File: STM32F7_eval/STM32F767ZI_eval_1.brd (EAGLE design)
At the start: 76.2 x 53.3 mm, 102 parts, among them CN1 STLINKV2_SWD_IF_, CN2 GROVE-4P-CONN-I2C-90D, CN3 GROVE-4P-CONN-I2C-90D, CN5 ARDUINO_COMPAT_IF, CN7 WFT0750CZ09-SMD_, CN9 UART_IF, Q1 PMF370XN_, SW1 SKRPACE010_, SW2 SKRPACE010_, U1 STM32F767ZI_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

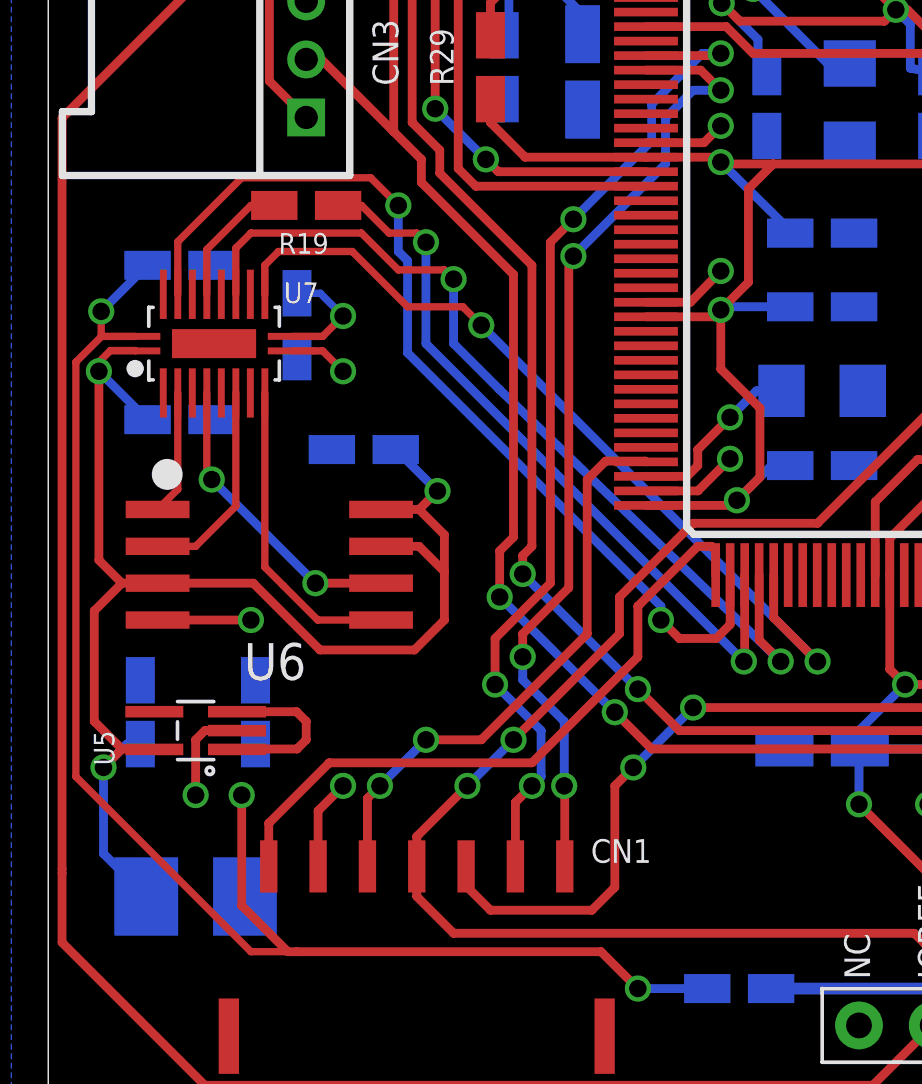
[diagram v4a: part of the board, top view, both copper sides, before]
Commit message: レイアウトを修正
・デザインルールチェック済み第１版
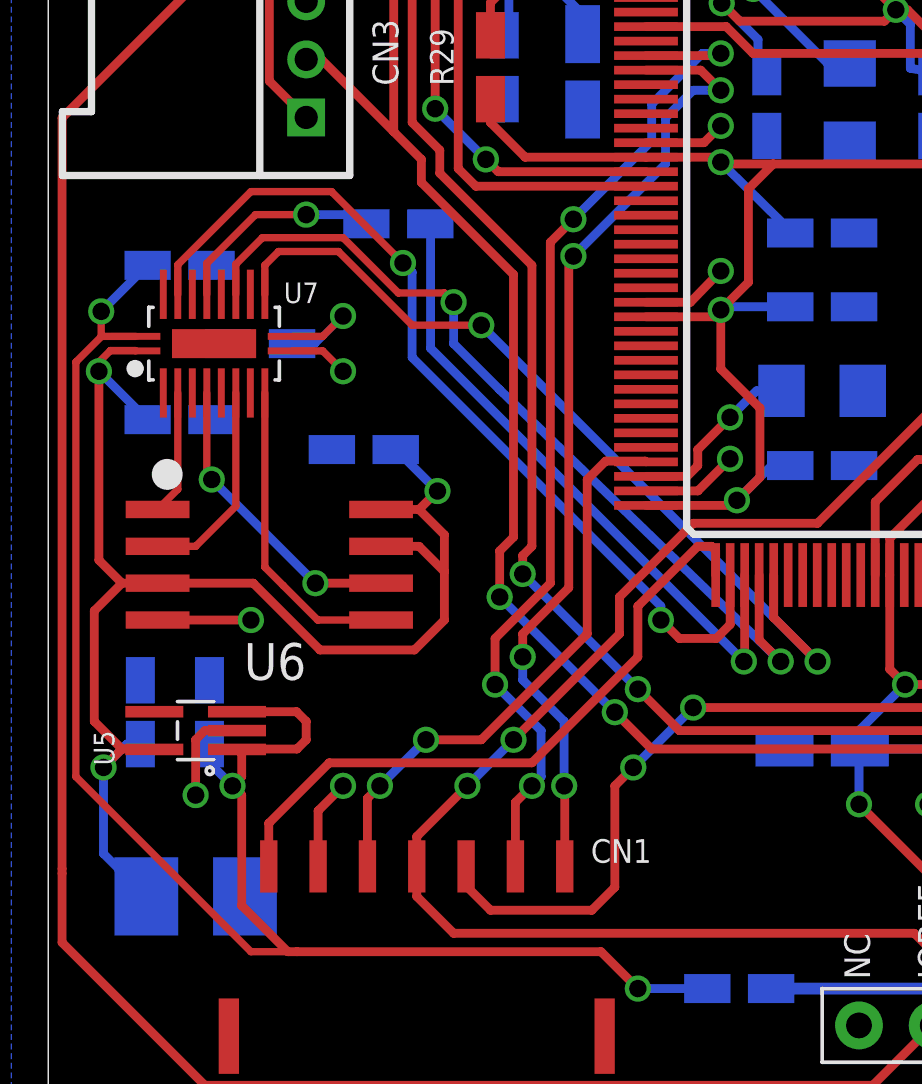
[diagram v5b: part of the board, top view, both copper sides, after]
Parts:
- moved R19 3.24 mm to (12.1, 30.2), flipped to the bottom, turned to 180 degrees
- moved C49 1.59 mm to (5.56, 13.3)
- moved R5 1.42 mm to (7.30, 26.0), turned to 180 degrees
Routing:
- net VCC_MEM: track 56.7 -> 60.4 mm
- net PC10: track 25.5 -> 22.5 mm, vias 2 -> 1
- net PC10_D: track 4.50 -> 7.39 mm, vias 0 -> 1
- net PA15: track 33.3 -> 31.4 mm
- net PC11: track 31.2 -> 30.3 mm

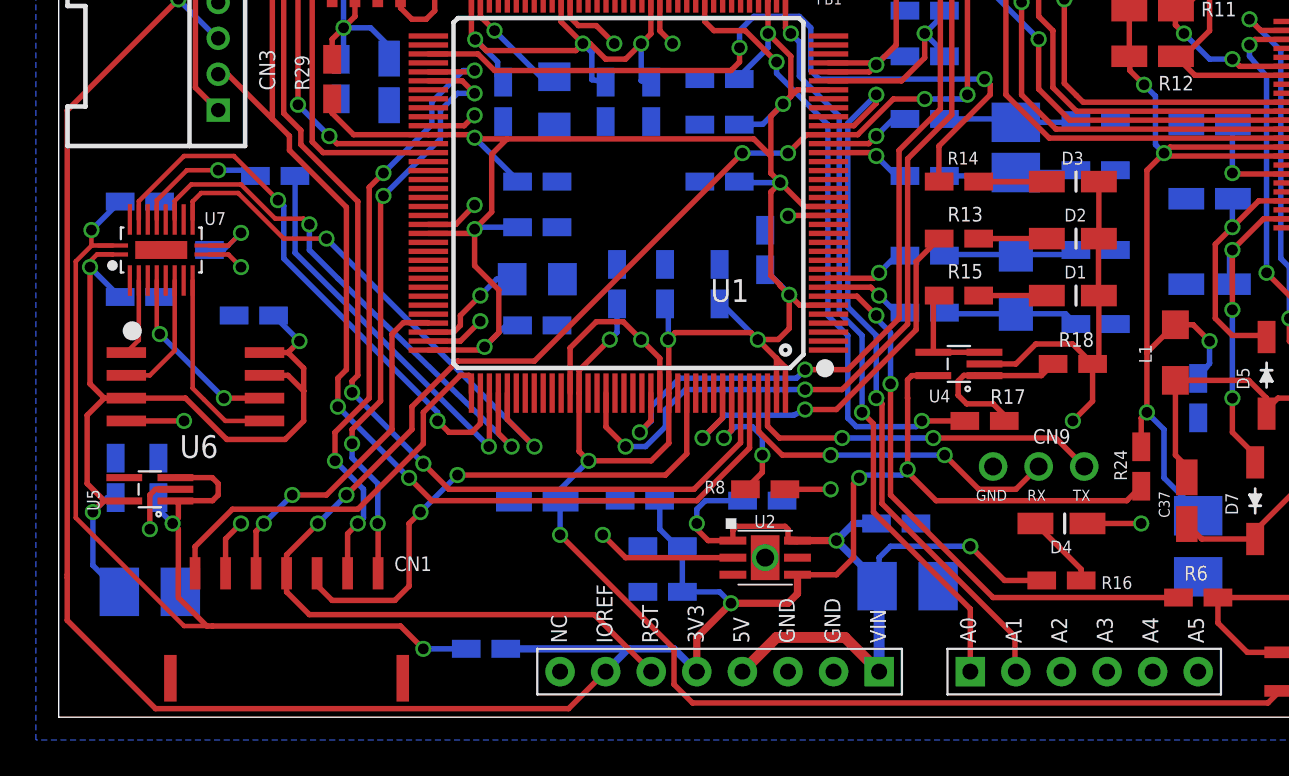
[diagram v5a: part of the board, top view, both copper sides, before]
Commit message: レイアウトを修正
・通信モジュール用のUARTピンの位置を変更
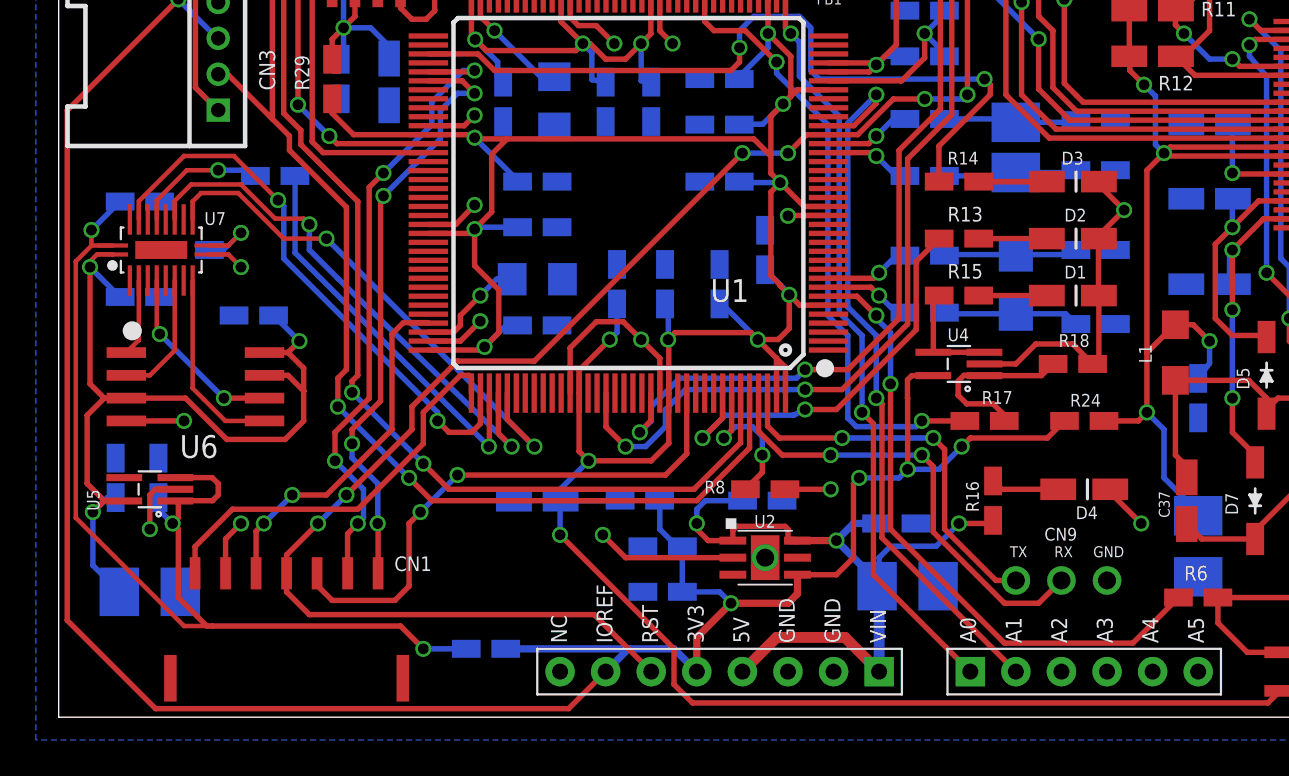
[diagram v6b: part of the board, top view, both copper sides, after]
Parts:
- moved CN9 8.98 mm to (58.4, 7.62), turned to 180 degrees
- moved R16 5.85 mm to (52.1, 12.1), turned to 270 degrees
- moved R24 4.07 mm to (57.1, 16.5), turned to 0 degrees
- moved D4 2.29 mm to (57.1, 12.7)
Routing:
- net PE0: track 19.6 -> 25.6 mm
- net +3V3: track 147.0 -> 143.2 mm, vias 4 -> 5
- net PC13: track 31.8 -> 35.1 mm
- net VIN: track 47.1 -> 44.2 mm
- net 0V: track 175.5 -> 172.6 mm
- net PE1: track 20.4 -> 21.8 mm
- net VCC_EPD: track 60.1 -> 60.6 mm

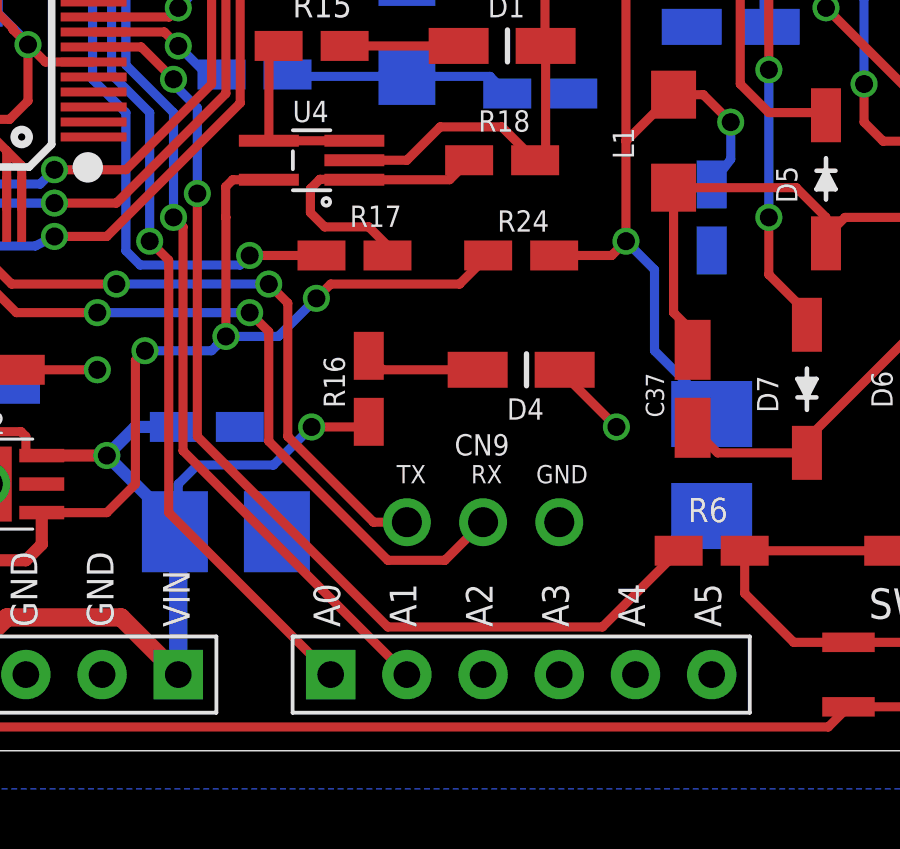
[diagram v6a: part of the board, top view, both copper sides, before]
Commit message: レイアウトを修正
・外部RX、TXはArduinoアナログピンを流用させるよう実装変更
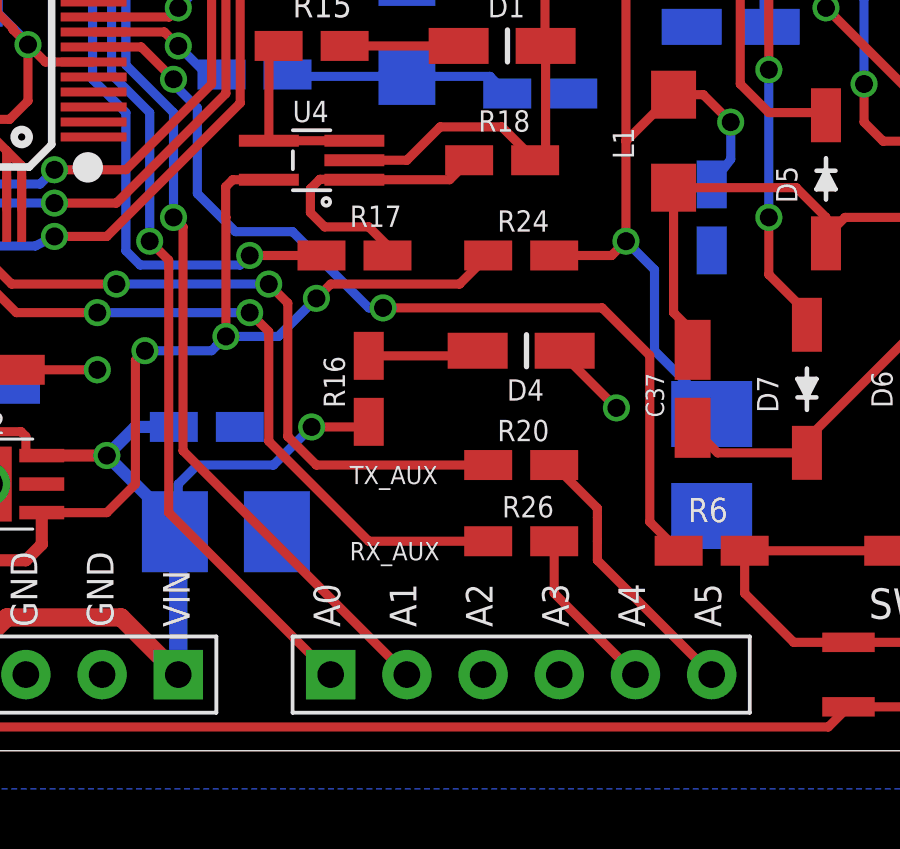
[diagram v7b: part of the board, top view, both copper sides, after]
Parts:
- removed CN9: UART_IF, PartsForProto:UART_IF_3PIN
- added R20, R26: 0, Parts:SMD_1608_DEV
- moved D4 0.64 mm to (57.1, 13.3)
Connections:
- new net RX_AUX: CN5.31, R26.1
- new net TX_AUX: CN5.32, R20.1
- net 0V: no longer CN9.1
- net PE0: now also R26.2; no longer CN9.2
- net PE1: now also R20.2; no longer CN9.3
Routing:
- net TX_AUX: track 0.00 -> 9.16 mm
- net RX_AUX: track 0.00 -> 5.57 mm
- net PC13: track 35.1 -> 31.5 mm
- net PE1: track 21.8 -> 23.8 mm
- net 0V: track 172.6 -> 171.5 mm
- net PE0: track 25.6 -> 25.0 mm
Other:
- board text added: "RX_AUX"
- board text added: "TX_AUX"
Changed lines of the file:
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@@
 <setting verticaltext="up"/>
 </settings>
-<grid distance="0.05" unitdist="inch" unit="inch" style="lines" multiple="1" display="yes" altdistance="0.025" altunitdist="inch" altunit="inch"/>
+<grid distance="0.05" unitdist="inch" unit="mil" style="lines" multiple="1" display="yes" altdistance="0.025" altunitdist="inch" altunit="inch"/>
 <layers>
 <layer number="1" name="Top" color="4" fill="1" visible="yes" active="yes"/>
@@
 <circle x="42.70375" y="19.446875" radius="0.508" width="0" layer="21"/>
 <circle x="63.02375" y="43.259375" radius="0.4064" width="0" layer="21"/>
+<text x="51.435" y="8.89" size="0.6096" layer="25">TX_AUX</text>
+<text x="51.435" y="6.35" size="0.6096" layer="25">RX_AUX</text>
 </plain>
 <attributes>
@@
 <attribute name="VALUE" x="50.8" y="25.4" size="0.8128" layer="27" rot="R180"/>
 </element>
-<element name="D4" library="Parts" package="CHIPLED_0805" value="LED_0805" x="57.15" y="12.7" smashed="yes">
-<attribute name="NAME" x="56.67375" y="11.7475" size="0.7112" layer="25" align="top-left"/>
-<attribute name="VALUE" x="54.61" y="11.1125" size="0.7112" layer="27"/>
+<element name="D4" library="Parts" package="CHIPLED_0805" value="LED_0805" x="57.15" y="13.335" smashed="yes">
+<attribute name="NAME" x="56.67375" y="12.3825" size="0.7112" layer="25" align="top-left"/>
+<attribute name="VALUE" x="54.61" y="11.7475" size="0.7112" layer="27"/>
 </element>
 <element name="R16" library="Parts" package="SMD_1608_DEV" value="1k" x="52.07" y="12.065" smashed="yes" rot="R270">
@@
 <attribute name="NAME" x="56.35625" y="17.30375" size="0.7112" layer="25"/>
 <attribute name="VALUE" x="56.515" y="14.605" size="0.8128" layer="27"/>
-</element>
-<element name="CN9" library="PartsForProto" package="UART_IF_3PIN" value="UART_IF" x="58.42" y="7.62" smashed="yes" rot="R180">
-<attribute name="NAME" x="54.9275" y="9.8425" size="0.7112" layer="25" ratio="10"/>
-<attribute name="VALUE" x="59.3725" y="10.795" size="0.8128" layer="27" rot="R180"/>
 </element>
 <element name="C39" library="Parts" package="C1210_TPST_DEV" value="10uF" x="63.5" y="9.525" smashed="yes" rot="MR270">
@@
 <element name="CN2" library="PartsForProto" package="GROVE-4P-90D" value="GROVE-4P-CONN-I2C-90D" x="8.89" y="47.9425" rot="R90"/>
 <element name="CN3" library="PartsForProto" package="GROVE-4P-90D" value="GROVE-4P-CONN-I2C-90D" x="8.89" y="36.83" rot="R90"/>
+<element name="R20" library="Parts" package="SMD_1608_DEV" value="0" x="57.15" y="9.525" smashed="yes" rot="R180">
+<attribute name="NAME" x="56.35625" y="10.31875" size="0.7112" layer="25"/>
+<attribute name="VALUE" x="57.785" y="11.43" size="0.8128" layer="27" rot="R180"/>
+</element>
+<element name="R26" library="Parts" package="SMD_1608_DEV" value="0" x="57.15" y="6.985" smashed="yes" rot="R180">
+<attribute name="NAME" x="56.515" y="7.77875" size="0.7112" layer="25"/>
+<attribute name="VALUE" x="57.785" y="8.89" size="0.8128" layer="27" rot="R180"/>
+</element>
 </elements>
 <signals>
@@
 <wire x1="29.96" y1="38.54" x2="30.96" y2="37.54" width="0.3048" layer="1"/>
 <via x="40.64" y="27.94" extent="1-16" drill="0.6"/>
-<wire x1="49.0075" y1="7.3025" x2="49.53" y2="8.255" width="0.6096" layer="16"/>
 <wire x1="72.91" y1="51.875" x2="68.06" y2="51.875" width="0.3048" layer="1"/>
 <via x="74.295" y="5.3975" extent="1-16" drill="0.6"/>
@@
 <contactref element="C38" pad="2"/>
 <contactref element="D6" pad="1"/>
-<contactref element="CN9" pad="1"/>
 <wire x1="74.295" y1="36.195" x2="74.295" y2="37.465" width="0.3048" layer="1"/>
 <wire x1="70.485" y1="9.93" x2="73.46" y2="9.93" width="0.3048" layer="1"/>
@@
 <contactref element="CN2" pad="4"/>
 <contactref element="CN3" pad="4"/>
-<via x="60.325" y="10.795" extent="1-16" drill="0.6"/>
+<via x="60.325" y="11.43" extent="1-16" drill="0.6"/>
 <via x="43.02125" y="12.7" extent="1-16" drill="0.6"/>
 <wire x1="40.47" y1="12.7" x2="43.02125" y2="12.7" width="0.3048" layer="1"/>
@@
 <wire x1="57.965" y1="26.67" x2="57.965" y2="26.85" width="0.3048" layer="1"/>
 <wire x1="57.965" y1="26.85" x2="59.3725" y2="28.2575" width="0.3048" layer="1"/>
-<wire x1="60.325" y1="10.795" x2="58.6" y2="12.52" width="0.3048" layer="1"/>
-<wire x1="58.6" y1="12.52" x2="58.6" y2="12.7" width="0.3048" layer="1"/>
+<wire x1="58.6" y1="13.335" x2="58.6" y2="13.155" width="0.3048" layer="1"/>
+<wire x1="58.6" y1="13.155" x2="60.325" y2="11.43" width="0.3048" layer="1"/>
 </signal>
 <signal name="N$2">
@@
 <contactref element="R6" pad="1"/>
 <via x="45.56125" y="22.38375" extent="1-16" drill="0.6"/>
-<via x="46.355" y="18.57375" extent="1-16" drill="0.6"/>
 <wire x1="46.355" y1="21.43125" x2="46.355" y2="18.57375" width="0.3048" layer="16"/>
 <wire x1="45.56125" y1="22.38375" x2="45.56125" y2="22.225" width="0.3048" layer="16"/>
@@
 <wire x1="42.9" y1="23.46" x2="44.485" y2="23.46" width="0.3048" layer="1"/>
 <wire x1="44.485" y1="23.46" x2="45.56125" y2="22.38375" width="0.3048" layer="1"/>
-<wire x1="46.355" y1="18.57375" x2="46.355" y2="10.4775" width="0.3048" layer="1"/>
-<wire x1="46.355" y1="10.4775" x2="52.705" y2="4.1275" width="0.3048" layer="1"/>
-<wire x1="52.705" y1="4.1275" x2="59.86" y2="4.1275" width="0.3048" layer="1"/>
-<wire x1="59.86" y1="4.1275" x2="62.4" y2="6.6675" width="0.3048" layer="1"/>
+<wire x1="62.4" y1="6.6675" x2="61.43625" y2="7.63125" width="0.3048" layer="1"/>
+<wire x1="61.43625" y1="7.63125" x2="61.43625" y2="13.17625" width="0.3048" layer="1"/>
+<wire x1="61.43625" y1="13.17625" x2="59.84875" y2="14.76375" width="0.3048" layer="1"/>
+<wire x1="59.84875" y1="14.76375" x2="52.54625" y2="14.76375" width="0.3048" layer="1"/>
+<via x="52.54625" y="14.76375" extent="1-16" drill="0.6"/>
+<wire x1="52.54625" y1="14.76375" x2="52.07" y2="14.76375" width="0.3048" layer="16"/>
+<wire x1="52.07" y1="14.76375" x2="49.53" y2="17.30375" width="0.3048" layer="16"/>
+<wire x1="49.53" y1="17.30375" x2="47.625" y2="17.30375" width="0.3048" layer="16"/>
+<wire x1="47.625" y1="17.30375" x2="46.355" y2="18.57375" width="0.3048" layer="16"/>
 </signal>
 <signal name="AGND">
@@
 <contactref element="R16" pad="1"/>
 <contactref element="D4" pad="A"/>
-<wire x1="52.07" y1="13.165" x2="52.535" y2="12.7" width="0.3048" layer="1"/>
-<wire x1="52.535" y1="12.7" x2="55.7" y2="12.7" width="0.3048" layer="1"/>
+<wire x1="52.07" y1="13.165" x2="55.53" y2="13.165" width="0.3048" layer="1"/>
+<wire x1="55.53" y1="13.165" x2="55.7" y2="13.335" width="0.3048" layer="1"/>
 </signal>
 <signal name="LED1">
@@
 <wire x1="43.65625" y1="15.5575" x2="40.16375" y2="15.5575" width="0.3048" layer="1"/>
 <wire x1="40.16375" y1="15.5575" x2="39.5" y2="16.22125" width="0.3048" layer="1"/>
-<contactref element="CN9" pad="3"/>
 <wire x1="48.73625" y1="15.5575" x2="49.37125" y2="14.9225" width="0.3048" layer="1"/>
 <wire x1="49.37125" y1="14.9225" x2="49.37125" y2="10.4775" width="0.3048" layer="1"/>
-<wire x1="49.37125" y1="10.4775" x2="52.22875" y2="7.62" width="0.3048" layer="1"/>
-<wire x1="52.22875" y1="7.62" x2="53.34" y2="7.62" width="0.3048" layer="1"/>
+<contactref element="R20" pad="2"/>
+<wire x1="56.05" y1="9.525" x2="50.32375" y2="9.525" width="0.3048" layer="1"/>
+<wire x1="50.32375" y1="9.525" x2="49.37125" y2="10.4775" width="0.3048" layer="1"/>
 </signal>
 <signal name="PE0">
@@
 <wire x1="43.02125" y1="14.605" x2="40.3225" y2="14.605" width="0.3048" layer="1"/>
 <wire x1="40.3225" y1="14.605" x2="39" y2="15.9275" width="0.3048" layer="1"/>
-<contactref element="CN9" pad="2"/>
 <wire x1="48.10125" y1="14.605" x2="48.73625" y2="13.97" width="0.3048" layer="1"/>
 <wire x1="48.73625" y1="13.97" x2="48.73625" y2="10.31875" width="0.3048" layer="1"/>
-<wire x1="48.73625" y1="10.31875" x2="52.705" y2="6.35" width="0.3048" layer="1"/>
-<wire x1="52.705" y1="6.35" x2="54.61" y2="6.35" width="0.3048" layer="1"/>
-<wire x1="54.61" y1="6.35" x2="55.88" y2="7.62" width="0.3048" layer="1"/>
+<contactref element="R26" pad="2"/>
+<wire x1="56.05" y1="6.985" x2="52.07" y2="6.985" width="0.3048" layer="1"/>
+<wire x1="52.07" y1="6.985" x2="48.73625" y2="10.31875" width="0.3048" layer="1"/>
 </signal>
 <signal name="VCC_EPD">
@@
 <wire x1="7.14375" y1="30.48" x2="8.89" y2="30.48" width="0.254" layer="1"/>
 </signal>
+<signal name="TX_AUX">
+<contactref element="CN5" pad="32"/>
+<contactref element="R20" pad="1"/>
+<wire x1="63.5" y1="2.54" x2="59.69" y2="6.35" width="0.3048" layer="1"/>
+<wire x1="59.69" y1="6.35" x2="59.69" y2="6.985" width="0.3048" layer="1"/>
+<wire x1="59.69" y1="6.985" x2="59.69" y2="7.77875" width="0.3048" layer="1"/>
+<wire x1="58.25" y1="9.525" x2="59.69" y2="8.085" width="0.3048" layer="1"/>
+<wire x1="59.69" y1="8.085" x2="59.69" y2="7.77875" width="0.3048" layer="1"/>
+</signal>
+<signal name="RX_AUX">
+<contactref element="CN5" pad="31"/>
+<contactref element="R26" pad="1"/>
+<wire x1="60.96" y1="2.54" x2="58.25" y2="5.25" width="0.3048" layer="1"/>
+<wire x1="58.25" y1="5.25" x2="58.25" y2="6.985" width="0.3048" layer="1"/>
+</signal>
 </signals>
